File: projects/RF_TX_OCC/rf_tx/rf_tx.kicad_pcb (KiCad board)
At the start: 2 copper layers, 44.5 x 31.8 mm, 14 parts, among them J1 Conn_01x03, J2 Conn_01x03, J3 Conn_01x04, J4 Conn_01x01_Female, SW1 SW_DIP_x08, SW2 SW_DIP_x04, U1 74LVC1G04, U2 74LVC1G14, U3 74LVC1G86, U4 HT12E

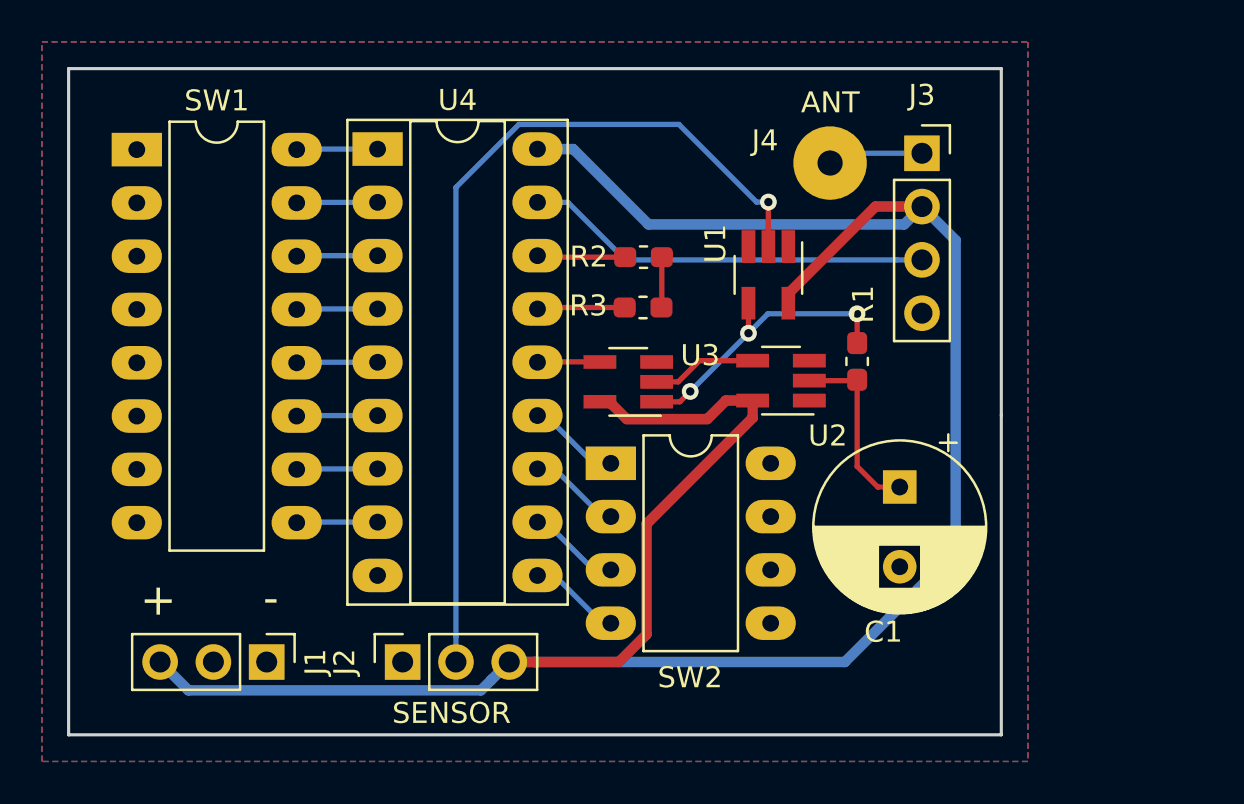
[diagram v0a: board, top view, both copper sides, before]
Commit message: RF TX for the PIR sensor
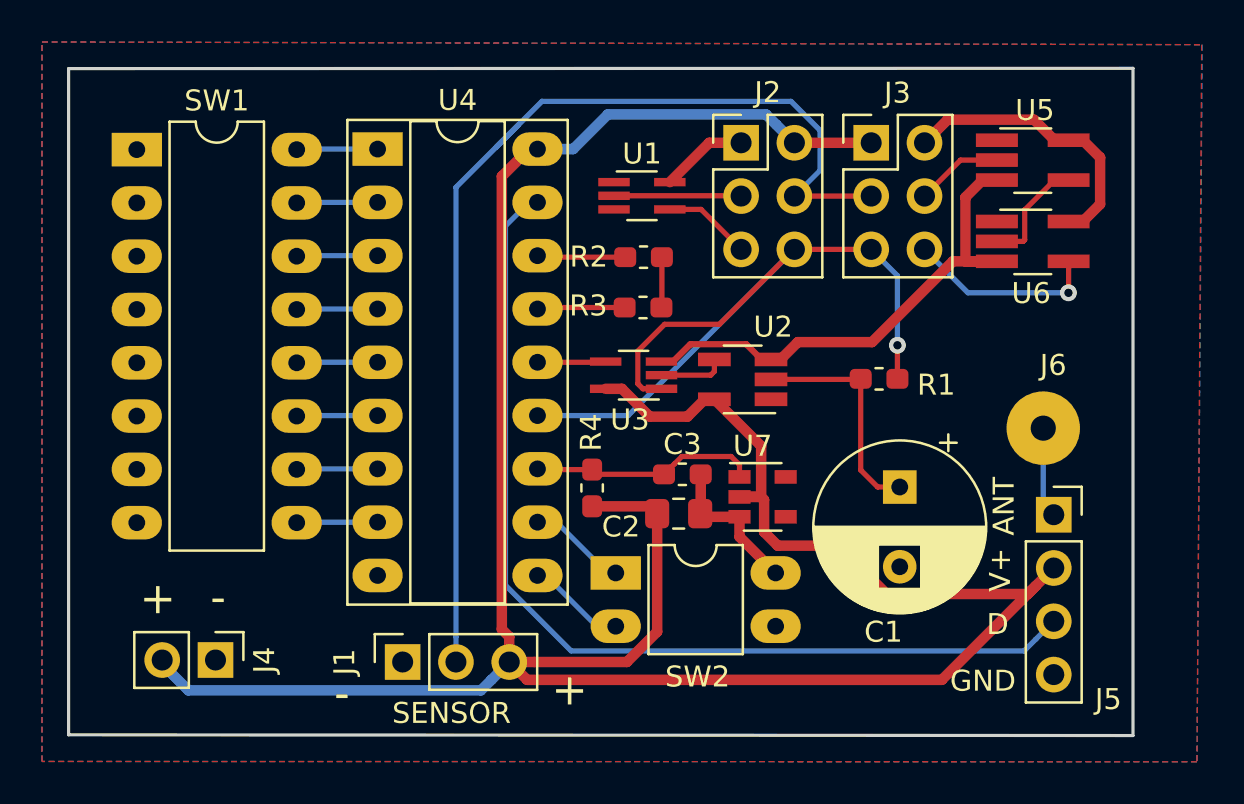
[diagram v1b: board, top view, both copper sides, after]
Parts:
- removed the J1 at (92.0, 100.7)
- added C2: 1uF, Capacitor_SMD:C_0805_2012Metric_Pad1.15x1.40mm_HandSolder, F.Cu at (111.6, 93.6)
- added C3: 30pF, Capacitor_SMD:C_0603_1608Metric_Pad1.05x0.95mm_HandSolder, F.Cu at (111.8, 91.7)
- added J2: Conn_02x03_Odd_Even, Connector_PinHeader_2.54mm:PinHeader_2x03_P2.54mm_Vertical, F.Cu at (114.6, 75.9)
- added J3: Conn_02x03_Odd_Even, Connector_PinHeader_2.54mm:PinHeader_2x03_P2.54mm_Vertical, F.Cu at (120.8, 75.9)
- added J4: Conn_01x02, Connector_PinHeader_2.54mm:PinHeader_1x02_P2.54mm_Vertical, F.Cu at (89.5, 100.6)
- added R4: 470K, Resistor_SMD:R_0603_1608Metric_Pad1.05x0.95mm_HandSolder, F.Cu at (107.5, 92.4)
- added U5: 74LVC1G04, Package_TO_SOT_SMD:TSOT-23-5_HandSoldering, F.Cu at (128.5, 76.8)
- added U6: 74LVC1G04, Package_TO_SOT_SMD:TSOT-23-5_HandSoldering, F.Cu at (128.5, 80.6)
- added U7: BD48ExxG, Package_TO_SOT_SMD:SOT-23-5, F.Cu at (115.6, 92.8)
- SW2: value SW_DIP_x04 -> SW_DIP_x02; footprint Package_DIP:DIP-8_W7.62mm_LongPads -> Package_DIP:DIP-4_W7.62mm_LongPads
- U1: value 74LVC1G04 -> 74LVC1G125; footprint Package_TO_SOT_SMD:SOT-23-5_HandSoldering -> Package_TO_SOT_SMD:SOT-353_SC-70-5_Handsoldering
- U3: footprint Package_TO_SOT_SMD:SOT-23-5_HandSoldering -> Package_TO_SOT_SMD:SOT-353_SC-70-5_Handsoldering
- moved J5 18.3 mm to (129.5, 93.7)
- moved J6 16.2 mm to (129.0, 89.5)
- moved U1 7.11 mm to (109.9, 78.5), turned to 0 degrees
- moved SW2 5.23 mm to (108.6, 96.4)
- moved U2 1.83 mm to (114.7, 87.2)
- moved R1 1.33 mm to (121.2, 87.2), turned to 180 degrees
- moved U3 0.41 mm to (109.5, 87.0)
- renumbered J2 to J1, J3 to J5, J4 to J6
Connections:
- R1 pad 1: Net-(R1-Pad1) -> /OUT
- SW2 pad 3: Net-(SW2-Pad3) -> GND
- SW2 pad 4: Net-(SW2-Pad4) -> GND
- U1 pad 1: (no net) -> GND
- U1 pad 2: /SENSOR -> Net-(J2-Pad3)
- U1 pad 4: Net-(R1-Pad1) -> Net-(J2-Pad5)
- U1 pad 5: VCC -> Net-(J2-Pad1)
- U3 pad 1: Net-(R1-Pad1) -> /OUT
- U4 pad 10: Net-(SW2-Pad4) -> Net-(SW2-Pad2)
- U4 pad 11: Net-(SW2-Pad3) -> Net-(SW2-Pad1)
- U4 pad 12: Net-(SW2-Pad2) -> /BAT_LOW
- U4 pad 13: Net-(SW2-Pad1) -> /OUT
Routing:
- net /OUT: track 0.00 -> 38.5 mm, vias 0 -> 1
- net GND: track 0.00 -> 32.2 mm
- net /DATA: track 19.5 -> 47.1 mm
- net VCC: track 115.3 -> 136.1 mm
- net Net-(R1-Pad1): track 14.1 -> 0.00 mm, vias 3 -> 0
- net Net-(J3-Pad2): track 0.00 -> 13.6 mm
- net /BAT_LOW: track 0.00 -> 11.7 mm
- net Net-(J3-Pad6): track 0.00 -> 9.22 mm, vias 0 -> 1
- net /SENSOR: track 42.4 -> 51.1 mm, vias 1 -> 0
- net Net-(J2-Pad3): track 0.00 -> 6.06 mm
- net Net-(U5-Pad4): track 0.00 -> 5.47 mm
- net Net-(SW2-Pad3): track 4.44 -> 0.00 mm
- net Net-(SW2-Pad4): track 4.44 -> 0.00 mm
- net Net-(J2-Pad5): track 0.00 -> 4.18 mm
- net Net-(J2-Pad1): track 0.00 -> 4.17 mm
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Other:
- board size 44.5 x 31.8 mm -> 50.7 x 31.8 mm
- board text added: "D"
- board text added: "GND"
- board text added: "V+"
